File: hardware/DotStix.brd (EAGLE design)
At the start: 21.3 x 50.8 mm, 11 parts, among them U1 ATMEGA328P-MU-QFN32

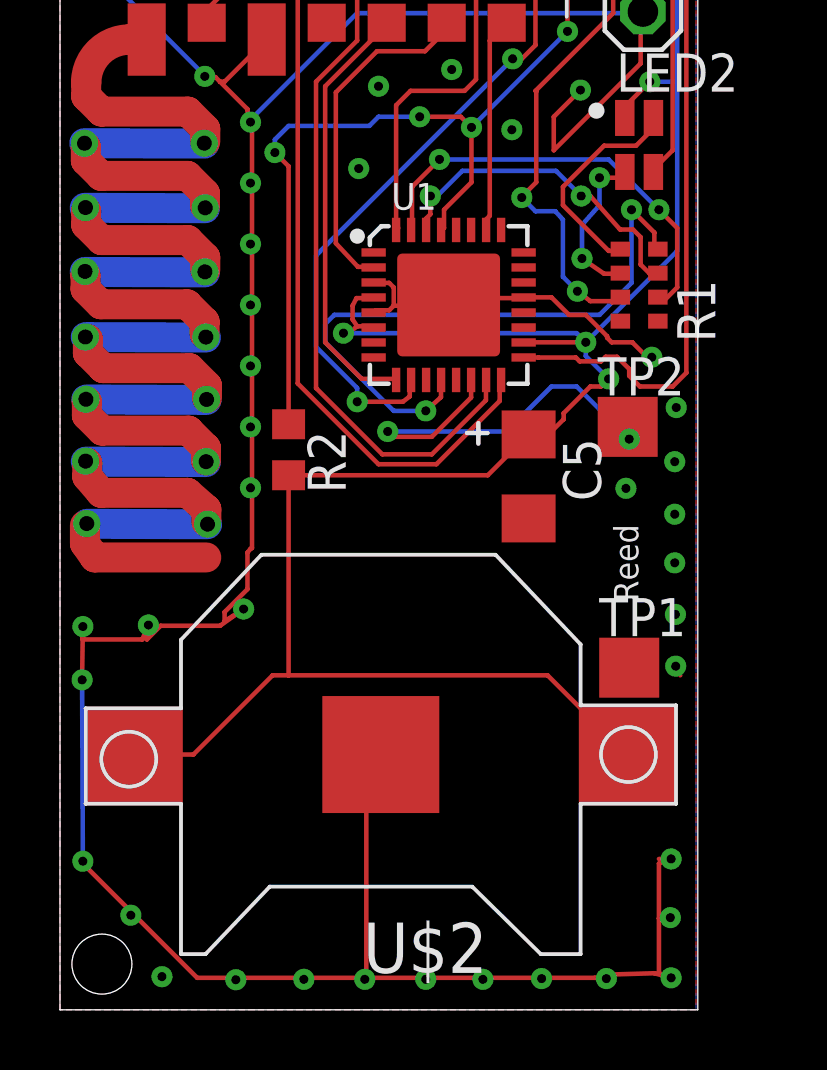
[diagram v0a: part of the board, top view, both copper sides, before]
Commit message: Add RST switch
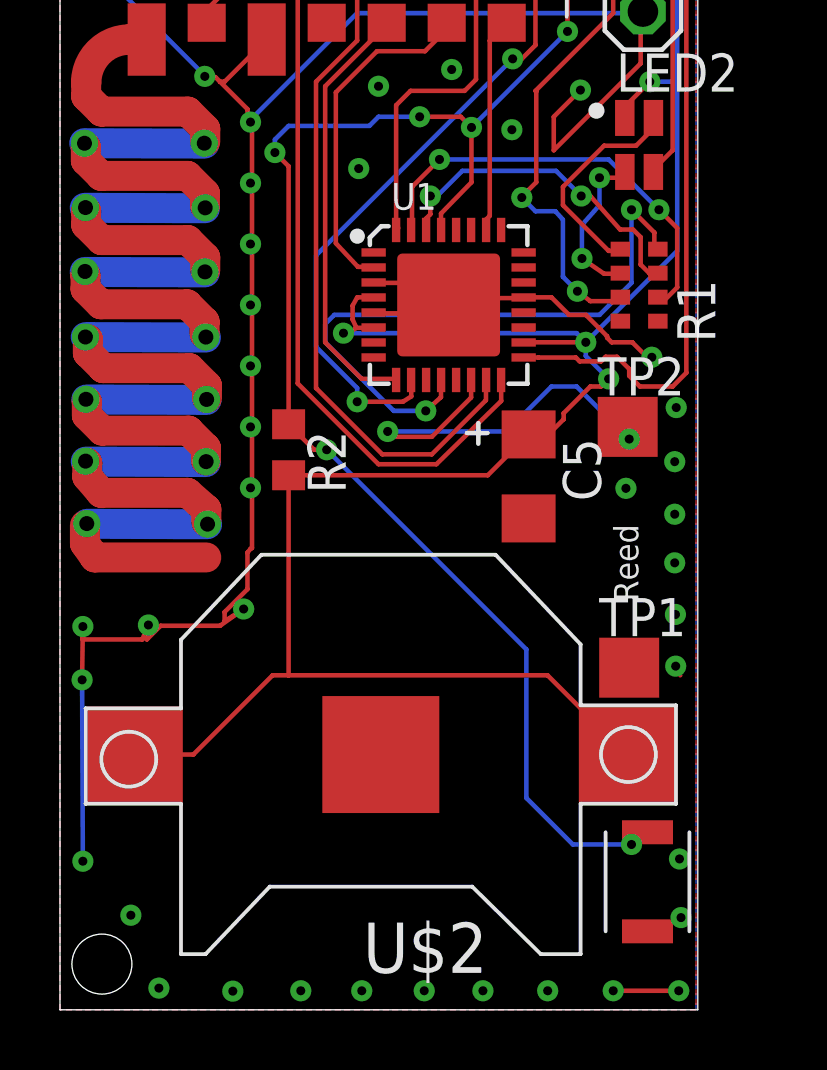
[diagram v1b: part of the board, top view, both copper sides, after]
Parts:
- added U$3: PUSHBUTTON_4X2.5, pusbbutton_4x2_5:PUSHBUTTON_4X2.5
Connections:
- net GND: now also U$3.P$2
- net RST: now also U$3.P$1
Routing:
- net GND: track 128.8 -> 98.6 mm
- net RST: track 31.8 -> 52.8 mm, vias 4 -> 6

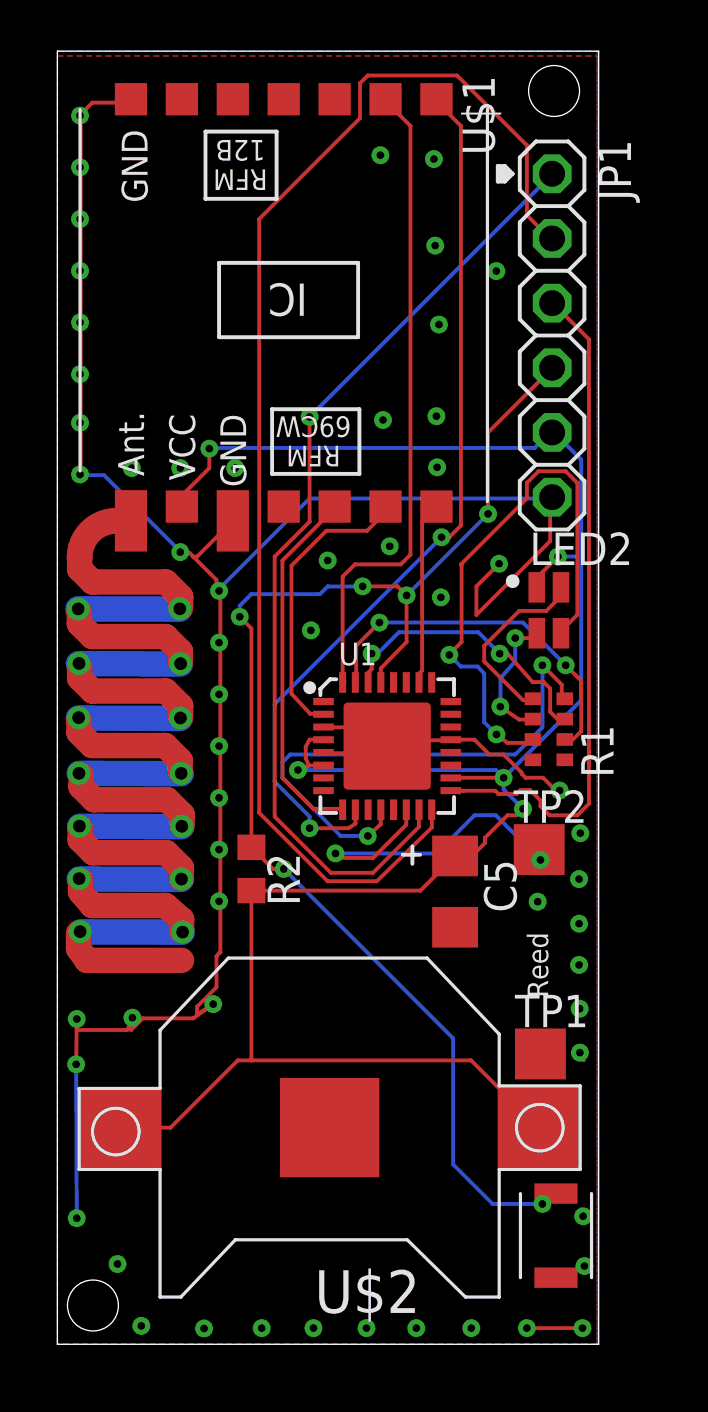
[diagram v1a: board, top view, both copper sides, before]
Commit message: Major rework, add solar cell
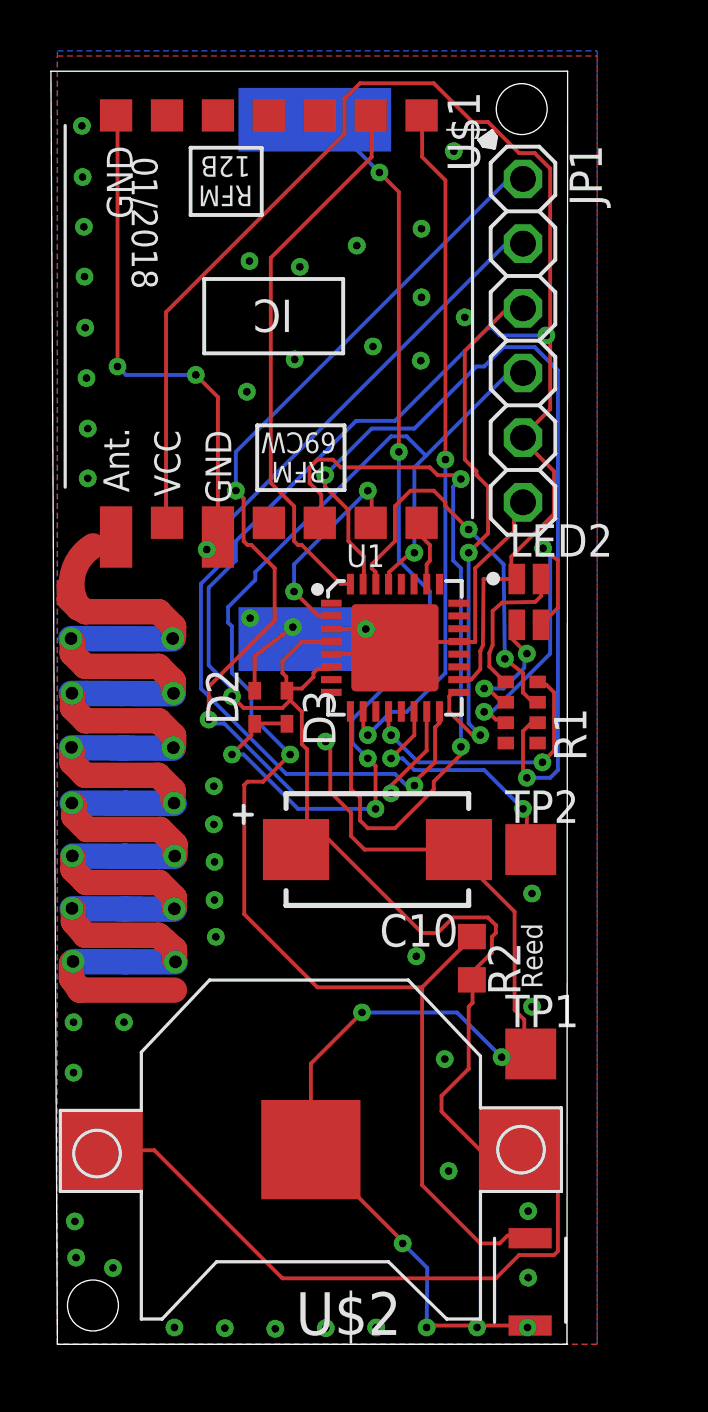
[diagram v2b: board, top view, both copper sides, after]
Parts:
- removed C5: 100uF 4V, adafruit:C3216
- added C10: 1500uF 4V, adafruit:CT7343
- added D1: SOLAR-IXYS-, SparkFun:SOLARBIT-12X1
- added D2, D3: (no value), diode:SOD523
- moved R2 9.34 mm to (16.3, 15.2)
- moved U1 3.87 mm to (13.3, 27.4)
- moved LOGO1 3.21 mm to (10.0, 13.9)
- moved U$3 2.03 mm to (18.6, 2.90)
- moved R1 1.25 mm to (18.2, 24.8)
- moved JP1 1.16 mm to (18.3, 39.4)
- moved U$2 1.14 mm to (9.96, 7.65)
- moved U$1 0.86 mm to (8.31, 40.8)
- moved LED2 0.85 mm to (18.5, 29.2)
- moved TP1 0.38 mm to (18.6, 11.4)
- moved TP2 0.33 mm to (18.6, 19.4)
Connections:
- new net SOLAR_RAW: D1.-, D2.C, D3.A
- net +3V3: now also C10.+, D3.C; no longer C5.1
- net GND: now also C10.-, D1.+, D2.A; no longer C5.2
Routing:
- net +3V3: track 87.6 -> 139.1 mm, vias 5 -> 2
- net SOLAR_RAW: track 0.00 -> 40.4 mm, vias 0 -> 5
- net TXD: track 14.5 -> 36.2 mm
- net RSDI: track 14.4 -> 29.8 mm, vias 0 -> 2
- net MISO: track 51.7 -> 36.5 mm, vias 0 -> 1
- net LED: track 21.2 -> 11.1 mm
- net N$5: track 22.4 -> 12.6 mm
- net GND: track 98.6 -> 89.3 mm, vias 57 -> 55
- net RSDO: track 35.2 -> 27.4 mm
- net RST: track 52.8 -> 60.3 mm, vias 6 -> 2
- net ANT: track 72.7 -> 79.8 mm
- net REED: track 15.4 -> 10.3 mm
- net SCK: track 26.5 -> 21.6 mm, vias 0 -> 2
- net RSEL: track 7.19 -> 2.59 mm
- net RXD: track 11.1 -> 15.4 mm
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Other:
- board size 21.3 x 50.8 mm -> 20.3 x 50 mm
- board text added: "DotStix v0.2.1"
- board text removed: "DotStix v0.1.1"
